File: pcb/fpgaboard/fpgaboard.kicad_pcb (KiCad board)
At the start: 4 copper layers, 140 x 140 mm, 342 parts, among them J1 CONN_02X02, J10 CONN_02X05, J11 Micro_SD_Card_Det_Hirose_DM3AT, J12 CONN_02X16, J13 CONN_02X16, J14 CONN_02X03, J15 GB_CARTRIDGE_CONN, J16 CONN_02X16, J17 CONN_02X16, J18 CONN_02X16, J19 CONN_02X03, J2 MICRO_USB, J20 CONN_02X05, J21 CONN_02X03, J22 CONN_02X05, J23 CONN_02X03, J24 CONN_02X03, J25 GBC_ELP, J26 CONN_02X05, J27 CONN_02X03, J28 SJ1-3533NG, J3 CONN_02X03, J4 CONN_01X02, J5 CONN_02X03, J6 CONN_01X21, J7 CONN_02X05, J8 CONN_02X05, J9 CONN_02X03, Q1 BSS138, Q2 BSS138, SW0 SW_Push, SW1 SW_Push, SW2 SW_Push, SW3 SW_Push, SW4 SW_DIP_x08, SW5 SW_DIP_x08, U1 LT3030EFE#TRPBF, U10 74LVCH8T245, U11 74LVCH8T245, U12 74LVCH8T245, U13 74LVCH8T245, U14 74LVCH8T245, U15 74LVCH8T245, U16 74LVCH8T245, U17 IS62WV1288BLL-55QLI, U18 IS62WV10248EBLL-45TLI, U19 74AHC1GU04, U2 W25Q32JVSSIM, U20 IS62WV1288BLL-55QLI, U21 IS62WV10248EBLL-45TLI, U22 IS62WV1288BLL-55QLI, U23 TDA7050, U24 TDA7050, U3 iCE40-HX8K-CT256, U4 93LC56B, U5 FT2232H, U6 74LVCH8T245, U7 74LVCH8T245, U8 74LVCH8T245, U9 74LVCH8T245, X1 12M, X2 16.777216M

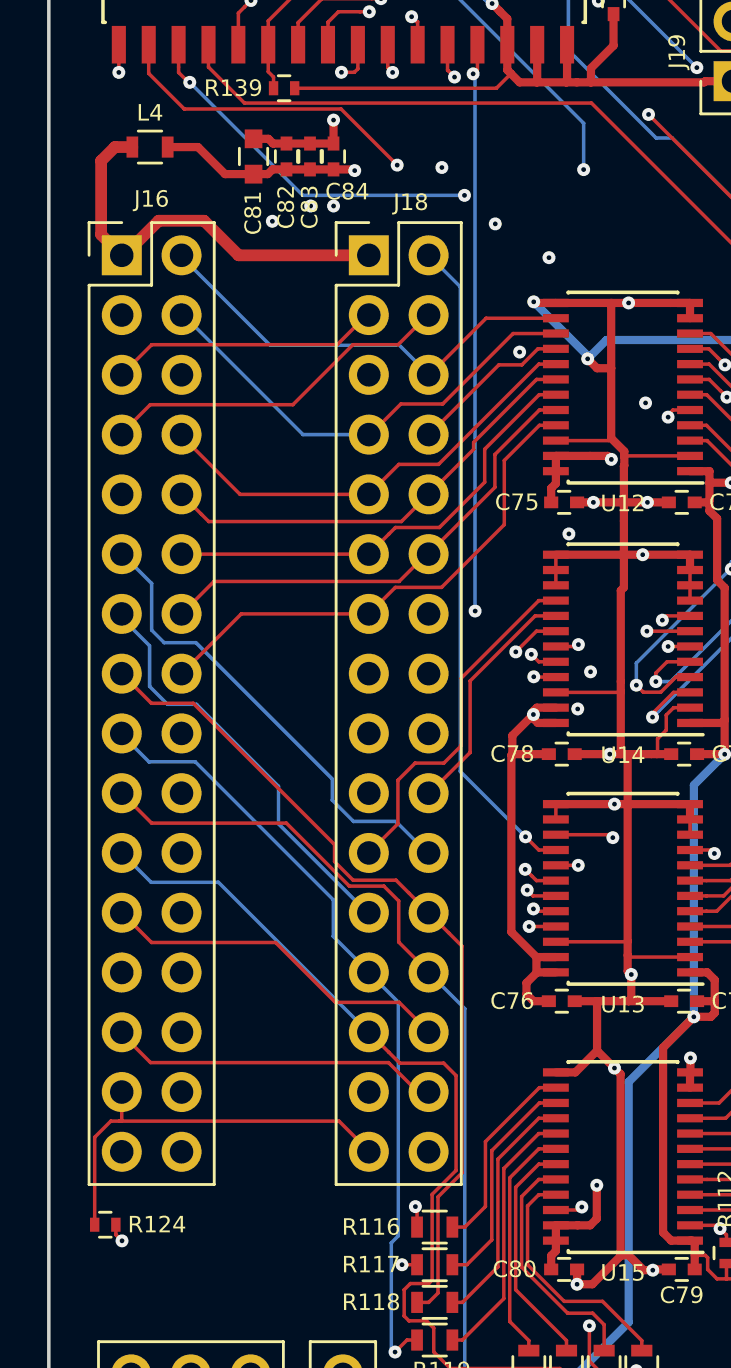
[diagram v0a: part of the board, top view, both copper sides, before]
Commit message: fix pin swap of gbreveng fpga board J16
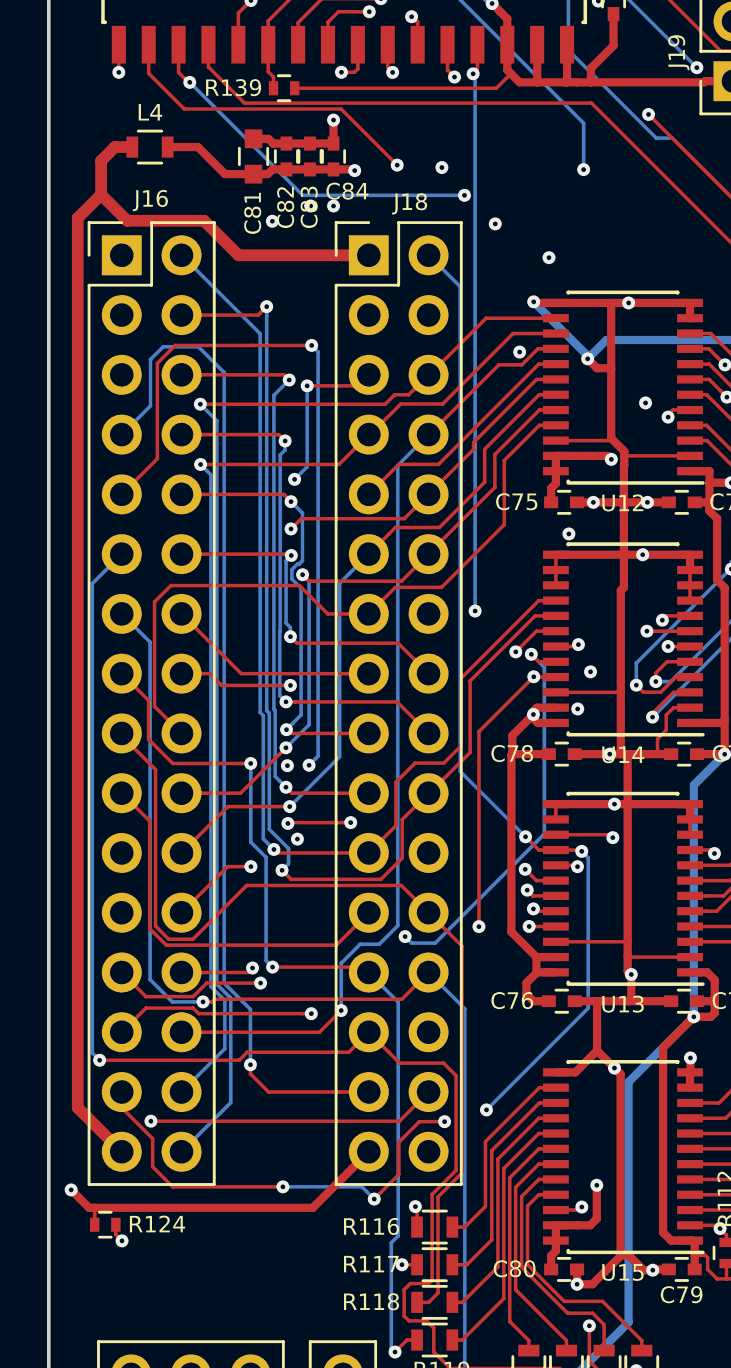
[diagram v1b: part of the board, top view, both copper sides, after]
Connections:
- J16 pad 1: /Cartridge Slave Slot/X_VCC -> GND
- J16 pad 10: /Cartridge Slave Slot/X_A4 -> /Cartridge Slave Slot/X_A11
- J16 pad 11: /Cartridge Slave Slot/X_D0 -> /Cartridge Slave Slot/X_D5
- J16 pad 12: /Cartridge Slave Slot/X_A5 -> /Cartridge Slave Slot/X_A10
- J16 pad 13: /Cartridge Slave Slot/X_D1 -> /Cartridge Slave Slot/X_D4
- J16 pad 14: /Cartridge Slave Slot/X_A6 -> /Cartridge Slave Slot/X_A9
- J16 pad 15: /Cartridge Slave Slot/X_D2 -> /Cartridge Slave Slot/X_D3
- J16 pad 16: /Cartridge Slave Slot/X_A7 -> /Cartridge Slave Slot/X_A8
- J16 pad 17: /Cartridge Slave Slot/X_D3 -> /Cartridge Slave Slot/X_D2
- J16 pad 18: /Cartridge Slave Slot/X_A8 -> /Cartridge Slave Slot/X_A7
- J16 pad 19: /Cartridge Slave Slot/X_D4 -> /Cartridge Slave Slot/X_D1
- J16 pad 2: /Cartridge Slave Slot/X_A0 -> /Cartridge Slave Slot/X_A15
- J16 pad 20: /Cartridge Slave Slot/X_A9 -> /Cartridge Slave Slot/X_A6
- J16 pad 21: /Cartridge Slave Slot/X_D5 -> /Cartridge Slave Slot/X_D0
- J16 pad 22: /Cartridge Slave Slot/X_A10 -> /Cartridge Slave Slot/X_A5
- J16 pad 23: /Cartridge Slave Slot/X_D6 -> /Cartridge Slave Slot/X_~CS
- J16 pad 24: /Cartridge Slave Slot/X_A11 -> /Cartridge Slave Slot/X_A4
- J16 pad 25: /Cartridge Slave Slot/X_D7 -> /Cartridge Slave Slot/X_~RD
- J16 pad 26: /Cartridge Slave Slot/X_A12 -> /Cartridge Slave Slot/X_A3
- J16 pad 27: /Cartridge Slave Slot/X_~RST -> /Cartridge Slave Slot/X_~WR
- J16 pad 28: /Cartridge Slave Slot/X_A13 -> /Cartridge Slave Slot/X_A2
- J16 pad 29: /Cartridge Slave Slot/X_AIN -> /Cartridge Slave Slot/X_CLK
- J16 pad 3: /Cartridge Slave Slot/X_CLK -> /Cartridge Slave Slot/X_AIN
- J16 pad 30: /Cartridge Slave Slot/X_A14 -> /Cartridge Slave Slot/X_A1
- J16 pad 31: GND -> /Cartridge Slave Slot/X_VCC
- J16 pad 32: /Cartridge Slave Slot/X_A15 -> /Cartridge Slave Slot/X_A0
- J16 pad 4: /Cartridge Slave Slot/X_A1 -> /Cartridge Slave Slot/X_A14
- J16 pad 5: /Cartridge Slave Slot/X_~WR -> /Cartridge Slave Slot/X_~RST
- J16 pad 6: /Cartridge Slave Slot/X_A2 -> /Cartridge Slave Slot/X_A13
- J16 pad 7: /Cartridge Slave Slot/X_~RD -> /Cartridge Slave Slot/X_D7
- J16 pad 8: /Cartridge Slave Slot/X_A3 -> /Cartridge Slave Slot/X_A12
- J16 pad 9: /Cartridge Slave Slot/X_~CS -> /Cartridge Slave Slot/X_D6
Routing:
- net GND: track 2183.9 -> 2235.4 mm
- net /Cartridge Slave Slot/X_VCC: track 17.7 -> 57.3 mm
- net /Cartridge Slave Slot/X_AIN: track 17.5 -> 52.7 mm, vias 0 -> 1
- net /Cartridge Slave Slot/X_D6: track 33.5 -> 66.1 mm, vias 1 -> 3
- net /Cartridge Slave Slot/X_A0: track 19.1 -> 49.8 mm, vias 0 -> 1
- net /Cartridge Slave Slot/X_~RST: track 42.8 -> 73.2 mm, vias 1 -> 2
- net /Cartridge Slave Slot/X_A1: track 19.8 -> 45.3 mm, vias 0 -> 1
- net /Cartridge Slave Slot/X_D7: track 38.0 -> 61.2 mm, vias 1 -> 2
- net /Cartridge Slave Slot/X_CLK: track 42.0 -> 62.8 mm, vias 1 -> 6
- net /Cartridge Slave Slot/X_~CS: track 33.4 -> 54.0 mm, vias 1 -> 5
- net /Cartridge Slave Slot/X_D5: track 38.7 -> 59.1 mm, vias 0 -> 1
- net /Cartridge Slave Slot/X_A2: track 20.6 -> 40.6 mm, vias 0 -> 1
- net /Cartridge Slave Slot/X_~WR: track 30.7 -> 49.8 mm, vias 1 -> 3
- net /Cartridge Slave Slot/X_A14: track 28.6 -> 47.4 mm, vias 0 -> 2
- net /Cartridge Slave Slot/X_~RD: track 33.6 -> 51.9 mm, vias 1 -> 3
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
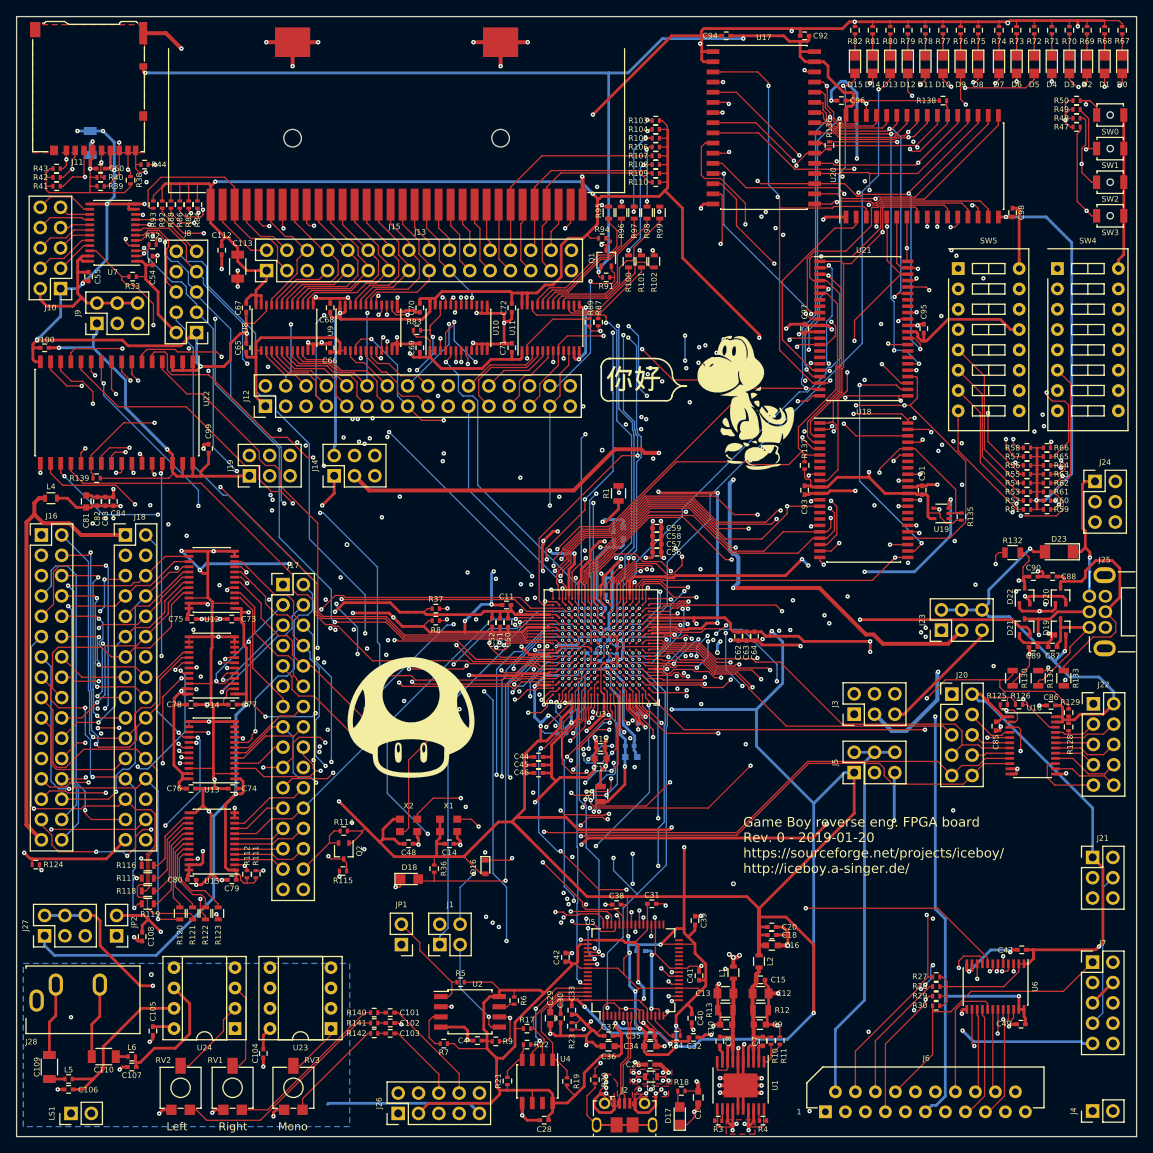
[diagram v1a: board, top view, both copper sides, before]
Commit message: label all external connector pins on gbreveng brd.
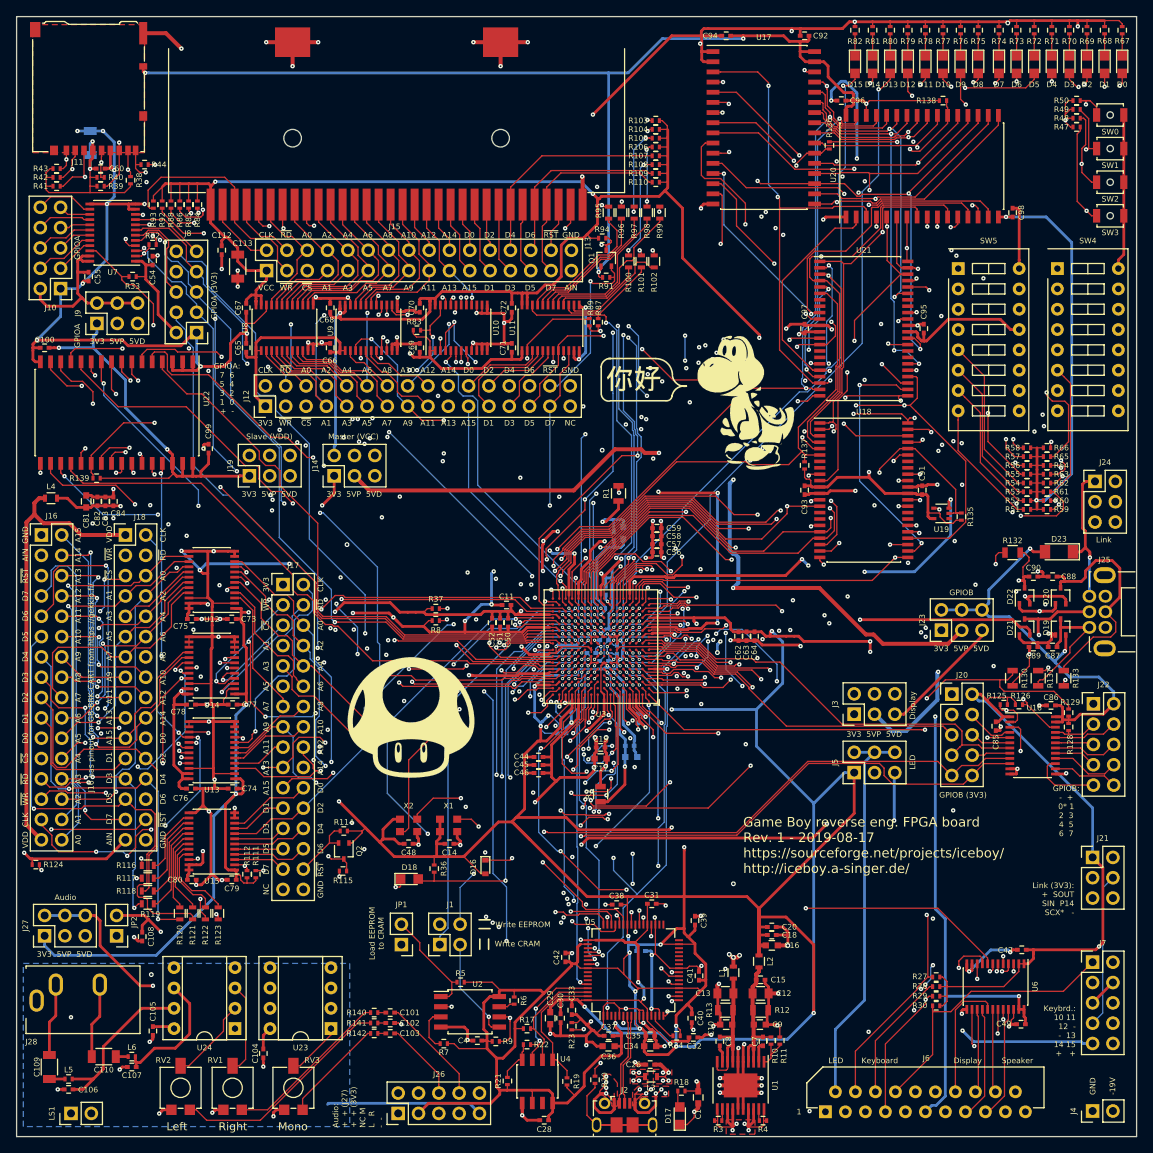
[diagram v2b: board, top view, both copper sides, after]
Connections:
- net /Cartridge Slave Slot/X_VCC renamed /Cartridge Slave Slot/X_VDD
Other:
- board text added: "-19V"
- board text added: "3V3"
- board text added: "3V3 5VP 5VD"
- board text added: "A0"
- board text added: "A1"
- board text added: "A10"
- board text added: "A11"
- board text added: "A12"
- board text added: "A13"
- board text added: "A14"
- board text added: "A15"
- board text added: "A2"
- board text added: "A3"
- board text added: "A4"
- board text added: "A5"
- board text added: "A6"
- board text added: "A7"
- board text added: "A8"
- board text added: "A9"
- board text added: "AIN"
- board text added: "Audio"
- board text added: "Audio: + + (J27) + + (3V3) NC M L R - -"
- board text added: "CLK"
- board text added: "D0"
- board text added: "D1"
- board text added: "D2"
- board text added: "D3"
- board text added: "D4"
- board text added: "D5"
- board text added: "D6"
- board text added: "D7"
- board text added: "Display"
- board text added: "GND"
- board text added: "GPIOA"
- board text added: "GPIOA (3V3)"
- board text added: "GPIOA: 7 6 5 4 3 2 1 0 + -"
- board text added: "GPIOB"
- board text added: "GPIOB (3V3)"
- board text added: "GPIOB: - + 0* 1 2 3 4 5 6 7"
- board text added: "Game Boy reverse eng. FPGA board Rev. 1 - 2019-08-17 https://sourceforge.net/projects/iceboy/ http://iceboy.a-singer.de/"
- board text added: "J16 has pinout for GB-BRK-CART from https://gekkio.fi/"
- board text added: "Keyboard"
- board text added: "Keybrd.: 10 11 12 - - 13 14 15 + +"
- board text added: "LED"
- board text added: "Link"
- board text added: "Link (3V3): + SOUT SIN P14 SCX* -"
- board text added: "Load EEPROM to CRAM"
- board text added: "Master (VCC)"
- board text added: "NC"
- board text added: "Slave (VDD)"
- board text added: "Speaker"
- board text added: "VCC"
- board text added: "VDD"
- board text added: "Write CRAM"
- board text added: "Write EEPROM"
- board text added: "~CS"
- board text added: "~RD"
- board text added: "~RST"
- board text added: "~WR"
- board text removed: "Game Boy reverse eng. FPGA board Rev. 0 - 2019-01-20 https://sourceforge.net/projects/iceboy/ http://iceboy.a-singer.de/"

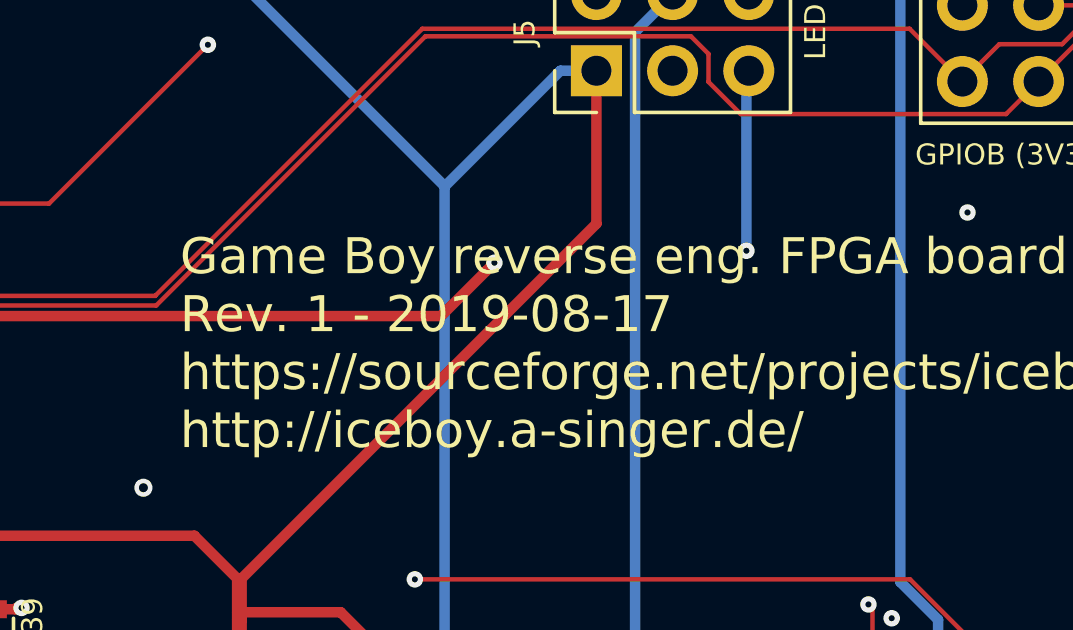
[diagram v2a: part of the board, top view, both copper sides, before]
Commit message: fix labeling of D0&D1 LCD signals
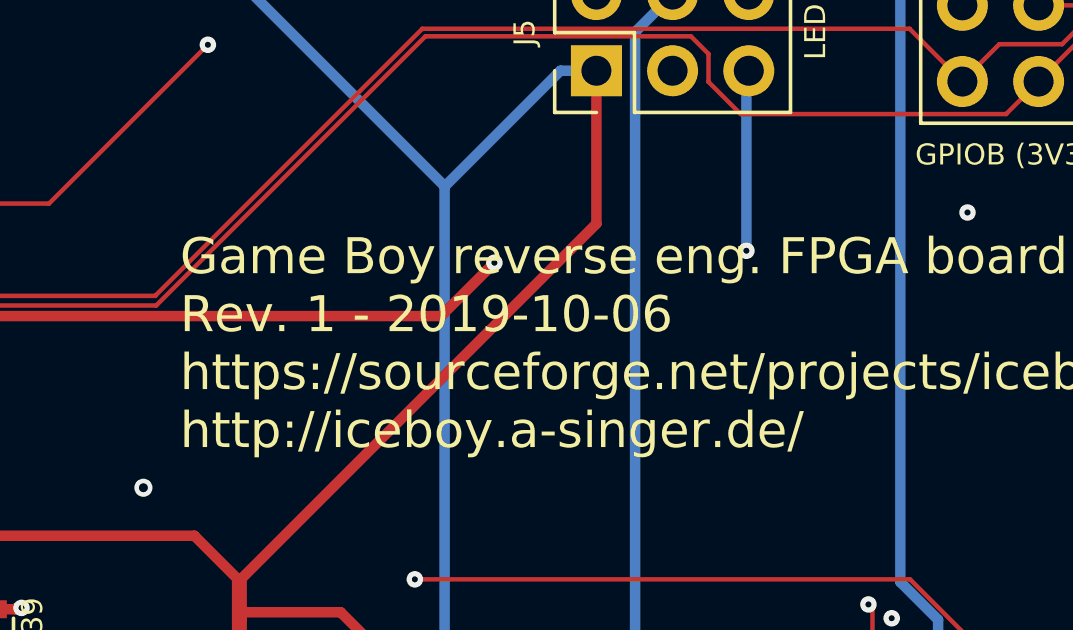
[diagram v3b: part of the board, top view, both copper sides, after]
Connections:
- J6 pad 15: /Bank0: Display, Keyboard, Clock/XDISP_D0 -> /Bank0: Display, Keyboard, Clock/XDISP_D1
- J6 pad 16: /Bank0: Display, Keyboard, Clock/XDISP_D1 -> /Bank0: Display, Keyboard, Clock/XDISP_D0
- U3 pad B5: /Bank0: Display, Keyboard, Clock/DISP_D1 -> /Bank0: Display, Keyboard, Clock/DISP_D0
- U3 pad E6: /Bank0: Display, Keyboard, Clock/DISP_D0 -> /Bank0: Display, Keyboard, Clock/DISP_D1
- U6 pad 15: /Bank0: Display, Keyboard, Clock/XDISP_D1 -> /Bank0: Display, Keyboard, Clock/XDISP_D0
- U6 pad 16: /Bank0: Display, Keyboard, Clock/XDISP_D0 -> /Bank0: Display, Keyboard, Clock/XDISP_D1
- U6 pad 8: /Bank0: Display, Keyboard, Clock/DISP_D0 -> /Bank0: Display, Keyboard, Clock/DISP_D1
- U6 pad 9: /Bank0: Display, Keyboard, Clock/DISP_D1 -> /Bank0: Display, Keyboard, Clock/DISP_D0
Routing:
- net /Bank0: Display, Keyboard, Clock/DISP_D1: track 63.5 -> 68.0 mm, vias 2 -> 3
- net /Bank0: Display, Keyboard, Clock/DISP_D0: track 68.0 -> 63.5 mm, vias 3 -> 2
- net /Bank0: Display, Keyboard, Clock/XDISP_D1: track 10.5 -> 14.2 mm
- net /Bank0: Display, Keyboard, Clock/XDISP_D0: track 14.2 -> 10.5 mm
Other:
- board text added: "Game Boy reverse eng. FPGA board Rev. 1 - 2019-10-06 https://sourceforge.net/projects/iceboy/ http://iceboy.a-singer.de/"
- board text removed: "Game Boy reverse eng. FPGA board Rev. 1 - 2019-08-17 https://sourceforge.net/projects/iceboy/ http://iceboy.a-singer.de/"

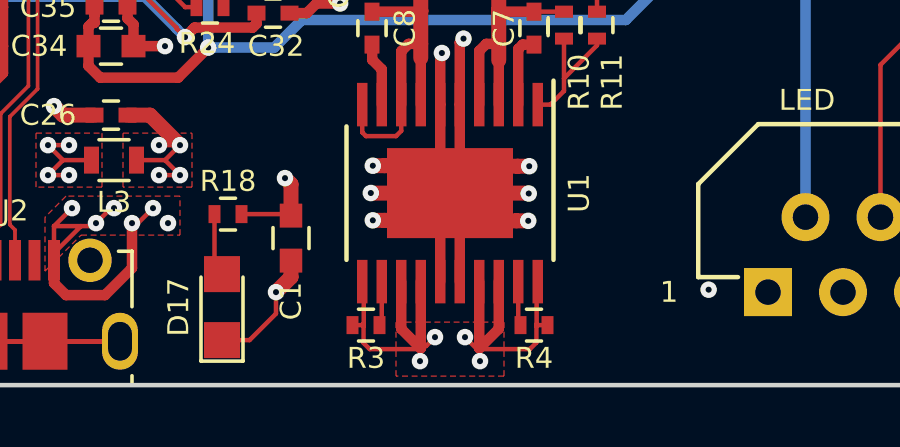
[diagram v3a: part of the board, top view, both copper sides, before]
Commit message: fix some ugly PCB traces
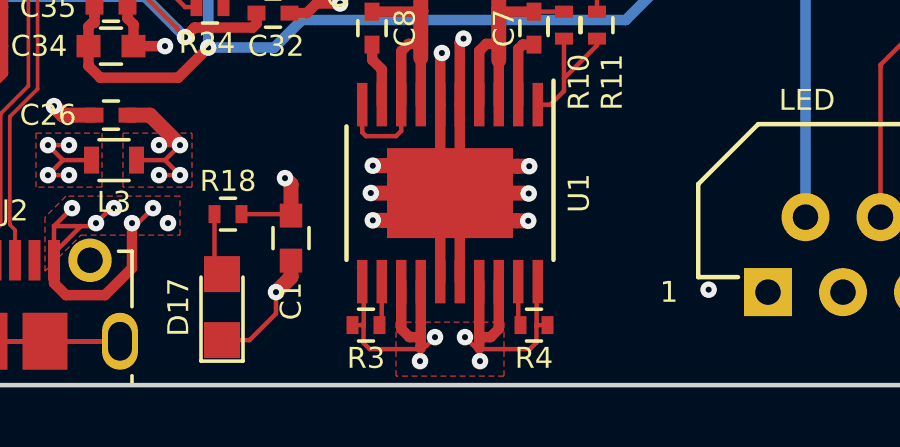
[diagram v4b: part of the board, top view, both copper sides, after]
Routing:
- net GND: track 2235.4 -> 2207.6 mm
- net +3V3: track 1861.6 -> 1860.2 mm
- net +1V2: track 219.1 -> 218.5 mm
